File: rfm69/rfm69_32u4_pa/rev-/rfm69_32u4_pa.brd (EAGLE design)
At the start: 69.8 x 69.8 mm, 38 parts, among them K1 G5LE, SW1 SPST_TACT-KMR2, U1 433MHz, X2 USB_B_PTH, Y1 8MHz

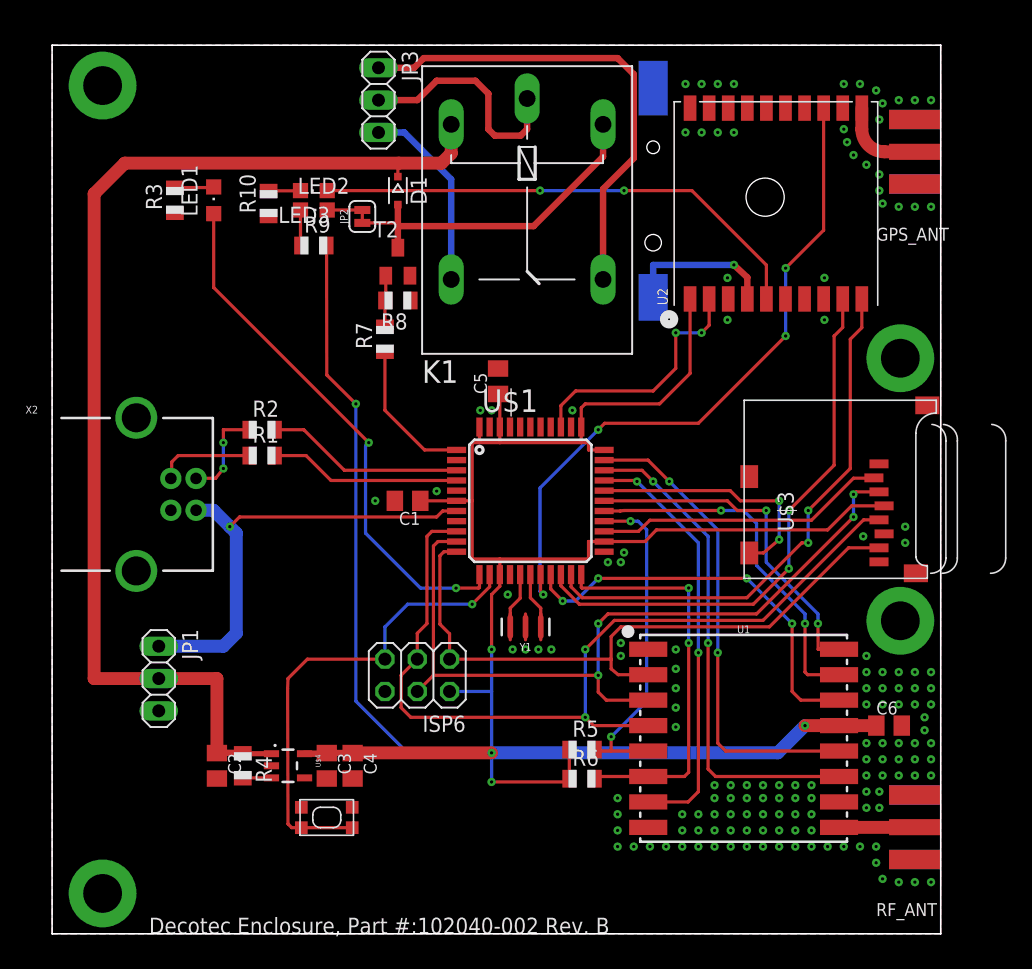
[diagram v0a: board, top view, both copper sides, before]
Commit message: New project, RFM69 with Mitsubishi MOSFET PA and PGA103 LNA and associated switching.  incomplete, but mostly done.
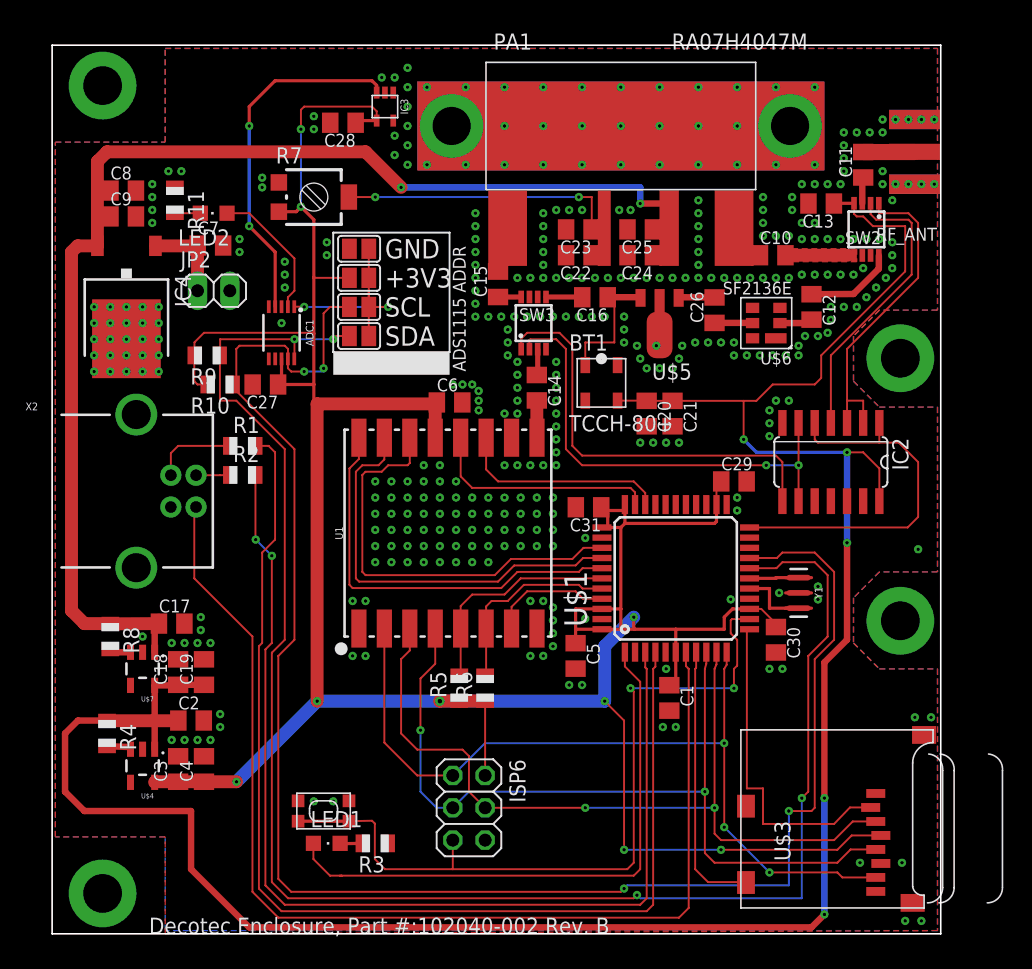
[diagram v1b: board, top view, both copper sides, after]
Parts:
- removed D1: 1N4148, diode:SOD323-R
- removed GPS_ANT: (no value), adafruit:SMA_EDGELAUNCH
- removed JP1, JP3: (no value), pinhead:1X03
- removed K1: G5LE, relay:G5LE
- removed LED3: FIX, adafruit:CHIPLED_0805
- removed T2: (no value), transistor:SOT23-BEC
- removed U2: (no value), adafruit:FGPMMOPA6H
- added ADC1: ADS1115, vtgs:MSOP10
- added BT1: TCCH-80+, kj4qlp:TCCH-80+
- added C10, C11, C12, C13, C14, C15, C16, C19, C20, C21, C26, C27, C28, C29, C30, C31, C9: 1uF, rcl:C0805K
- added C17, C18, C23, C25, C7, C8: 10uF, rcl:C0805K
- added C22, C24: .1uF, rcl:C0805K
- added IC2: 74HC04D, 74xx-eu:SO14
- added IC3: MCP9700, vtgs:SC70
- added IC4: 7812DT, adafruit:TO252
- added PA1: RA07H4047M, kj4qlp:H46
- added R11: 10K, adafruit:R0805
- added SJ1, SJ2, SJ3, SJ4: (no value), jumper:SJ
- added SW2: HMC574AMS8E, kj4qlp:MSOP8
- added SW3: HMC284AMS8G, kj4qlp:MSOP8
- added U$6: SF2136E, kj4qlp:SM3030-6
- added U$7: SPX3819M5_X_X, kj4qlp:SOT23-5
- JP2: value JUMPER-SMT_2_NC_TRACE_SILK -> (none); device SparkFun-Jumpers:SMT-JUMPER_2_NC_TRACE_SILK -> pinhead:1X02
- LED2: value RELAY -> (none)
- R10: value 10k -> 10K
- R7: value 1k -> (none); device adafruit:R0805 -> rcl:RTRIM3314G
- R8: value 10K -> 100K
- R9: value 1k -> 10K
- U$4: value SPX3819M5_3_3 -> SPX3819M5_X_X; device SparkFun-IC-Power:SOT23-5 -> kj4qlp:SOT23-5
- U$5: value CH291-1220LF -> PGA-103+; device battery:CH291-1220LF -> kj4qlp:SOT89
- moved RF_ANT 53.1 mm to (69.8, 61.5)
- moved R3 52.9 mm to (25.4, 7.11), turned to 180 degrees
- moved LED1 51.3 mm to (21.6, 7.11), turned to 270 degrees
- moved C6 42.9 mm to (31.2, 41.8)
- moved R8 34.8 mm to (4.57, 23.4), turned to 270 degrees
- moved U1 28.3 mm to (31.1, 31.5), turned to 90 degrees
- moved U$3 25.9 mm to (54.1, 2.03)
- moved C1 25.8 mm to (48.5, 18.5), turned to 270 degrees
- moved C5 22.4 mm to (41.1, 21.8), turned to 270 degrees
- moved Y1 21.6 mm to (58.7, 26.8), turned to 270 degrees
- moved R10 14.7 mm to (13.2, 43.2), turned to 180 degrees
- moved JP2 13.1 mm to (12.7, 50.5), turned to 0 degrees
- moved U$1 13.0 mm to (49.0, 27.9), turned to 90 degrees
- moved R7 12.5 mm to (20.6, 57.9), turned to 270 degrees
- moved R9 12.0 mm to (12.2, 45.5), turned to 180 degrees
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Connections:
- removed net 0_GPS_TXD: U$1.20, U2.P$9
- removed net 10_RF_DIO5: U$1.30, U1.7
- removed net 11_LED: LED1.A, U$1.12
- removed net 12_RF_CS: R5.2, U$1.26, U1.5
- removed net 1_GPS_RXD: U$1.21, U2.P$10
- removed net 22_RF_RST: R6.2, U$1.22, U1.6
- removed net 2_RF_DIO0: U$1.19, U1.14
- removed net 3D-FIX: LED3.A, U2.P$5
- removed net 3_GPS_PPS: U$1.18, U2.P$13
- removed net 4_SD_CS: U$1.25, U$3.2
- removed net 6_RF_DIO1: U$1.27, U1.15
- removed net 7_RELAY: R7.1, U$1.1
- removed net 8_RF_DIO2: U$1.28, U1.16
- removed net 9_SD_CD: U$1.29, U$3.CD1
- removed net A0_GPS_RST: U$1.36, U2.P$2
- removed net A1: U$1.37
- removed net A2: U$1.38
- removed net A3: U$1.39
- removed net A4: U$1.40
- removed net A5: U$1.41
- removed net RTCM: U2.P$14
- removed net V+: JP1.3
- removed net VBACKUP: U$5.+, U2.P$4
- removed net VIN: C2.1, D1.C, JP1.2, K1.1, R4.1, U$4.1
- new net +12V: C17.1, C24.1, C25.1, C8.1, C9.1, IC4.2, PA1.P$3, R8.1, U$7.1
- new net +5V: BT1.3, C13.1, C18.1, C19.1, C2.1, C20.1, C21.1, IC2.14, R4.1, SW2.4, U$4.1, U$7.5
- new net 10: U$1.30
- new net 11_SD_CS: U$1.12, U$3.2
- new net 12: U$1.26
- new net 22_TXRX_PTT: IC2.1, IC2.5, U$1.22
- new net 4: U$1.25
- new net 6: U$1.27
- new net 7_LED: LED1.A, U$1.1
- new net 8: U$1.28
- new net 8_SD_CD: U$1.8, U$3.CD1
- new net 9: U$1.29
- new net A0_RF_DIO0: U$1.36, U1.14
- new net A1_RF_DIO1: U$1.37, U1.15
- new net A2_RF_DIO2: U$1.38, U1.16
- new net A3_RF_CS: R5.2, U$1.39, U1.5
- new net A4_RF_RST: R6.2, U$1.40, U1.6
- new net A5_RF_DIO5: U$1.41, U1.7
- new net ADDR: ADC1.1, SJ1.1, SJ2.1, SJ3.1, SJ4.1
- new net ALERT: ADC1.2, LED2.A
- new net N$11: C11.2, RF_ANT.P
- new net N$15: C16.2, SW3.5
- new net N$16: IC2.8, SW3.1
- new net N$17: BT1.1, C16.1, U$5.3
- new net N$18: C22.1, C23.1, PA1.P$2, R7.2
- new net N$19: C12.1, SW2.8
- new net N$20: C12.2, U$6.2
- new net N$21: IC2.6, IC2.9, SW3.2
- new net N$22: C26.2, U$5.1
- new net N$23: R8.2, U$7.3
- new net N$24: LED2.C, R11.2
- new net N$6: C10.1, PA1.P$4
- new net RXD1: U$1.20
- new net SCL: ADC1.10, R9.1, SJ4.2, U$1.18
- new net SDA: ADC1.9, R10.1, SJ3.2, U$1.19
- new net TXD1: U$1.21
- new net V_PA_TEMP: ADC1.4, IC3.3
- net +3V3: now also ADC1.8, C27.1, C28.1, C29.1, C30.1, C31.1, IC3.4, R10.2, R7.1, SJ2.2; no longer U2.P$1
- net ANT: now also C14.2; no longer RF_ANT.P
- net GND: now also ADC1.3, C13.2, C17.2, C18.2, C19.2, C20.2, C21.2, C22.2, C23.2, C24.2, C25.2, C27.2, C28.2, C29.2, C30.2, C31.2, C7.2, C8.2, C9.2, IC2.7, IC3.1, IC3.2, IC3.5, IC4.3, JP2.2, PA1.P$5, PA1.P$6, PA1.P$7, PA1.P$8, R11.1, R7.3, SJ1.2, SW2.6, SW2.7, SW3.6, SW3.7, U$5.2, U$5.2@1, U$6.1, U$6.3, U$6.4, U$6.6, U$7.2; no longer GPS_ANT.GND@1, GPS_ANT.GND@2, GPS_ANT.GND@3, GPS_ANT.GND@4, R10.1, R8.1, T2.E, U$2.P$1, U$2.P$2, U$2.P$3, U$2.P$4, U$5.-, U2.P$12, U2.P$19, U2.P$3, U2.P$8
- net N$10: now also C26.1, U$6.5; no longer JP2.2, LED2.C
- net N$12: now also C11.1, SW2.3; no longer JP3.2, K1.P
- net N$13: now also C14.1, SW3.3; no longer JP3.1, K1.O
- net N$14: now also C15.1, SW3.8; no longer JP3.3, K1.S
- net N$4: now also C15.2, PA1.P$1; no longer D1.A, JP2.1, K1.2, T2.C
- net N$5: now also C7.1, IC4.1, JP2.1; no longer LED3.C, R10.2
- net N$7: now also C10.2, SW2.5; no longer GPS_ANT.P, U2.P$11
- net N$8: now also IC2.2, IC2.3, SW2.1; no longer R7.2, R8.2, T2.B
- net N$9: now also IC2.4, SW2.2; no longer LED2.A, R9.1
- net VBUS: no longer JP1.1
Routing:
- net +5V: track 0.00 -> 182.7 mm, vias 0 -> 5
- net SDA: track 0.00 -> 135.0 mm, vias 0 -> 4
- net SCL: track 0.00 -> 133.2 mm, vias 0 -> 4
- net +12V: track 0.00 -> 103.6 mm, vias 0 -> 2
- net VIN: track 91.1 -> 0.00 mm
- net D+: track 15.1 -> 88.4 mm
- net D-: track 15.6 -> 83.2 mm, vias 0 -> 2
- net 3_GPS_PPS: track 53.5 -> 0.00 mm, vias 4 -> 0
- net VBUS: track 36.6 -> 87.8 mm, vias 1 -> 0
- net 7_LED: track 0.00 -> 45.4 mm
- net 0_GPS_TXD: track 43.5 -> 0.00 mm, vias 2 -> 0
- net 1_GPS_RXD: track 42.7 -> 0.00 mm, vias 2 -> 0
- net 11_LED: track 42.0 -> 0.00 mm, vias 2 -> 0
- net 3D-FIX: track 39.6 -> 0.00 mm, vias 2 -> 0
- net N$21: track 0.00 -> 36.8 mm, vias 0 -> 2
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- added copper zone on layer 1, net N$7
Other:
- board text added: "+3V3"
- board text added: "ADS1115 ADDR"
- board text added: "GND"
- board text added: "SCL"
- board text added: "SDA"

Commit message: lots of detail updates, including test point additions, need to clean up silk screen.....
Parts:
- added D1: MBR120, adafruit:SOD-123
- added SJ5: (no value), jumper:SJ_2
- added TP-1, TP-10, TP-11, TP-12, TP-2, TP-3, TP-4, TP-5, TP-6, TP-7, TP-8, TP-9, TP1, TP10, TP11, TP12, TP13, TP14, TP15, TP2, TP3, TP4, TP5, TP6, TP7, TP8, TP9: TPSQTP10SQ, testpad:TP10SQ
- C20: value 1uF -> 0.33uF
- C21: value 1uF -> 10uF
- moved R1 9.27 mm to (16.5, 29.2), turned to 270 degrees
- moved R2 6.88 mm to (14.5, 29.2), turned to 270 degrees
- moved C20 3.39 mm to (43.4, 40.1), turned to 180 degrees
- moved C2 3.31 mm to (9.14, 14.0)
- moved C3 2.79 mm to (9.91, 10.2)
- moved C4 2.79 mm to (11.9, 10.2)
- moved U$4 2.79 mm to (7.11, 10.4)
- moved R4 2.79 mm to (4.32, 13.0)
- moved C21 2.30 mm to (46.5, 41.1), turned to 90 degrees
- moved ISP6 2.03 mm to (32.8, 11.9)
- moved C27 1.63 mm to (18.0, 42.2), turned to 270 degrees
- moved IC4 1.27 mm to (7.11, 49.3)
- moved R8 1.02 mm to (4.57, 24.4)
- moved U$7 1.02 mm to (7.11, 21.8)
- moved C17 1.02 mm to (9.40, 25.4)
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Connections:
- new net 5V_VREG: C18.1, C19.1, SJ5.3, U$7.5
- new net N$25: ADC1.5, TP1.TP
- new net N$26: ADC1.6, TP2.TP
- new net N$27: ADC1.7, TP3.TP
- net +3V3: now also TP11.TP, TP14.TP, TP5.TP
- net +5V: now also D1.C, SJ5.2, TP10.TP, TP15.TP; no longer C18.1, C19.1, U$7.5
- net 10: now also TP-10.TP
- net 12: now also TP8.TP
- net 13_RF_DIO4: now also TP-5.TP
- net 22_TXRX_PTT: now also TP-12.TP
- net 4: now also TP9.TP
- net 5_RF_DIO3: now also TP-4.TP
- net 6: now also TP7.TP
- net 8: now also TP-8.TP
- net 9: now also TP-9.TP
- net A0_RF_DIO0: now also TP-1.TP
- net A1_RF_DIO1: now also TP-2.TP
- net A2_RF_DIO2: now also TP-3.TP
- net A5_RF_DIO5: now also TP-6.TP
- net GND: now also TP12.TP, TP13.TP, TP4.TP, TP6.TP, U$2.P$1, U$2.P$2, U$2.P$3, U$2.P$4
- net RXD1: now also TP-11.TP
- net TXD1: now also TP-7.TP
- net VBUS: now also D1.A, SJ5.1
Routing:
- net 5_RF_DIO3: track 16.7 -> 37.1 mm, vias 0 -> 2
- net +3V3: track 235.4 -> 253.5 mm, vias 9 -> 13
- net 13_RF_DIO4: track 18.2 -> 35.9 mm, vias 0 -> 2
- net D+: track 88.4 -> 76.2 mm
- net TXD1: track 0.00 -> 12.0 mm
- net RXD1: track 0.00 -> 9.49 mm
- net 5V_VREG: track 0.00 -> 9.23 mm
- net 10: track 0.00 -> 8.88 mm, vias 0 -> 2
- net 6: track 0.00 -> 8.86 mm, vias 0 -> 2
- net A2_RF_DIO2: track 32.5 -> 41.2 mm, vias 0 -> 2
- net A1_RF_DIO1: track 32.9 -> 41.1 mm, vias 0 -> 2
- net N$1: track 6.62 -> 14.6 mm
- net D-: track 83.2 -> 75.6 mm
- net 12: track 0.00 -> 6.89 mm, vias 0 -> 2
- net 9: track 0.00 -> 6.87 mm, vias 0 -> 2
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
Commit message: Final version of Rev- board including Gerbers and Osh Park pictures.  This is the version sent to Osh PArk for fab.
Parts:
- removed JP2: (no value), pinhead:1X02
- removed LED2: (no value), adafruit:CHIPLED_0805
- removed SW3: HMC284AMS8G, kj4qlp:MSOP8
- removed TP-11, TP-7, TP13, TP9: TPSQTP10SQ, testpad:TP10SQ
- removed U$7: SPX3819M5_X_X, kj4qlp:SOT23-5
- removed X2: USB_B_PTH, SparkFun-Connectors:USB-B-PTH
- added AIN0, AIN1, AIN2, AIN3, DIO3, DIO5, GND@1, PTT, PTT1, PTT2, RXD1, SW1A, SW1B, SW2A, SW2B, TXD1, VGG: TPSQTP10SQ, testpad:TP10SQ
- added BTN1: SPST_TACT-KMR2, adafruit:KMR2
- added F1: 500mA, adafruit:R1206
- added GND, VIN: (no value), pinhead:1X01
- added LED-ALT, PTT-HI, PTT-LO, PWR: (no value), adafruit:CHIPLED_0805
- added R12, R13, R18: 10K, adafruit:R0805
- added R14, R15, R16, R17: 100, adafruit:R0805
- added TVS1: ESD8472, kj4qlp:X3DFN2
- added USB: USB_B_PTH, SparkFun-Connectors:USB-B-PTH
- added VR2: SPX3819M5_X_X, kj4qlp:SOT23-5
- C10, C11, C12, C15, C16, C26: value 1uF -> .01uF
- R3: value 10k -> 10K
- SW1: value SPST_TACT-KMR2 -> HMC284AMS8G; device adafruit:KMR2 -> kj4qlp:MSOP8
- TP3, TP7: value TPSQTP10SQ -> TPSQTP20SQ; device testpad:TP10SQ -> testpad:TP20SQ
- moved SW1 41.8 mm to (37.8, 48.0), turned to 0 degrees
- moved TP7 40.8 mm to (11.9, 51.1)
- moved TP-4 35.1 mm to (51.3, 38.4)
- moved TP8 29.8 mm to (26.9, 56.6)
- moved TP-6 25.9 mm to (51.3, 41.4)
- moved TP-12 19.1 mm to (51.3, 39.9)
- moved TP3 10.9 mm to (11.9, 53.8)
- moved R3 8.30 mm to (22.1, 14.7), turned to 270 degrees
- moved R11 6.27 mm to (15.0, 61.0)
- moved LED1 3.84 mm to (22.1, 10.9), turned to 0 degrees
- moved TP2 3.64 mm to (14.2, 48.5)
- moved TP1 2.41 mm to (14.2, 50.0)
- moved C7 2.05 mm to (14.2, 53.1), turned to 270 degrees
- moved C17 1.52 mm to (7.87, 25.4)
- moved R8 1.52 mm to (3.05, 24.4)
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- renumbered IC4 to VR1, TP-1 to DIO0, TP-2 to DIO1, TP-3 to DIO2, TP-5 to DIO4, U$1 to IC1, U$4 to VR3, U$5 to PGA-103+, U1 to RF1
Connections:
- new net AIN1: ADC1.5, AIN1.TP
- new net AIN2: ADC1.6, AIN2.TP
- new net AIN3: ADC1.7, AIN3.TP
- new net SW1A: IC2.8, R15.2, SW1A.TP
- new net SW1B: IC2.6, IC2.9, R14.2, SW1B.TP
- new net SW2A: IC2.2, IC2.3, R17.1, SW2A.TP
- new net SW2B: IC2.4, R16.1, SW2B.TP
- new net VIN: C7.1, TP3.TP, VIN.1, VR1.1
- new net VUSB: F1.1, USB.VBUS
- net +12V: now also VR2.1; no longer U$7.1
- net +3V3: now also PWR.A, R18.1, TP2.TP
- net 12: now also TP-12.TP; no longer TP8.TP
- net 22_TXRX_PTT: now also PTT.TP, PTT2.TP; no longer TP-12.TP
- net 4: now also TP-4.TP; no longer TP9.TP
- net 5V_VREG: now also VR2.5; no longer U$7.5
- net 5_RF_DIO3: now also DIO3.TP; no longer TP-4.TP
- net 6: now also TP-6.TP; no longer TP7.TP
- net A5_RF_DIO5: now also DIO5.TP; no longer TP-6.TP
- net ALERT: now also LED-ALT.A; no longer LED2.A
- net GND: now also BTN1.2, BTN1.4, GND.1, GND@1.TP, R12.1, R13.1, SW1.6, SW1.7, TP1.TP, TP7.TP, TP8.TP, TVS1.P$2, USB.GND, VR2.2; no longer JP2.2, SW1.2, SW1.4, SW3.6, SW3.7, TP13.TP, U$2.P$1, U$2.P$2, U$2.P$3, U$2.P$4, U$7.2, X2.GND
- net N$1: now also USB.D+; no longer X2.D+
- net N$11: now also TVS1.P$1
- net N$13: now also SW1.3; no longer SW3.3
- net N$14: now also SW1.8; no longer SW3.8
- net N$15: now also SW1.5; no longer SW3.5
- net N$16: now also R14.1, SW1.2; no longer IC2.8, SW3.1
- net N$18: now also VGG.TP
- net N$21: now also R15.1, SW1.1; no longer IC2.6, IC2.9, SW3.2
- net N$23: now also VR2.3; no longer U$7.3
- net N$24: now also LED-ALT.C; no longer LED2.C
- net N$25: now also R17.2, SW2.1; no longer ADC1.5, TP1.TP
- net N$26: now also R16.2, SW2.2; no longer ADC1.6, TP2.TP
- net N$27: now also PTT-LO.A, R18.2; no longer ADC1.7, TP3.TP
- net N$3: now also USB.D-; no longer X2.D-
- net N$5: now also PTT-HI.A, PTT-LO.C, PTT1.TP; no longer C7.1, JP2.1, VR1.1
- net N$8: now also PTT-HI.C, R12.2; no longer IC2.2, IC2.3, SW2.1
- net N$9: now also PWR.C, R13.2; no longer IC2.4, SW2.2
- net RST: now also BTN1.1, BTN1.3; no longer SW1.1, SW1.3
- net RXD1: now also RXD1.TP; no longer TP-11.TP
- net TXD1: now also TXD1.TP; no longer TP-7.TP
- net VBUS: now also F1.2; no longer X2.VBUS
- net V_PA_TEMP: now also AIN0.TP
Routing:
- net SW1A: track 0.00 -> 38.8 mm, vias 0 -> 2
- net N$21: track 36.8 -> 2.65 mm, vias 2 -> 0
- net SW1B: track 0.00 -> 32.5 mm, vias 0 -> 2
- net N$8: track 25.2 -> 1.76 mm
- net +3V3: track 253.5 -> 274.8 mm
- net N$9: track 22.7 -> 2.19 mm
- net N$16: track 33.7 -> 14.4 mm
- net N$26: track 1.29 -> 20.2 mm
- net N$25: track 2.01 -> 19.6 mm
- net SW2B: track 0.00 -> 11.8 mm, vias 0 -> 2
- net SW2A: track 0.00 -> 11.1 mm, vias 0 -> 2
- net VUSB: track 0.00 -> 11.0 mm
- net VBUS: track 92.3 -> 81.3 mm
- net VIN: track 0.00 -> 10.3 mm
- net N$11: track 4.07 -> 7.29 mm
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- added copper zone on layer 1, net N$10
- added copper zone on layer 1, net N$12
- added copper zone on layer 1, net N$14
- added copper zone on layer 1, net N$15
- added copper zone on layer 1, net N$19
- added copper zone on layer 1, net N$20
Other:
- board text added: "+5V"
- board text added: "MISO"
- board text added: "MOSI"
- board text added: "PN:"
- board text added: "RESET"
- board text added: "REV:"
- board text added: "RFM"
- board text added: "RST"
- board text added: "SCK"
- board text added: "SN:"
- board text added: "TP"
- board text added: "VBUS"
- board text added: "VREG"
- board text added: "uC TP"
